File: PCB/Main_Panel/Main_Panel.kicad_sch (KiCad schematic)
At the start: 2 parts, among them U1 Pico, U2 TLC5947DAP

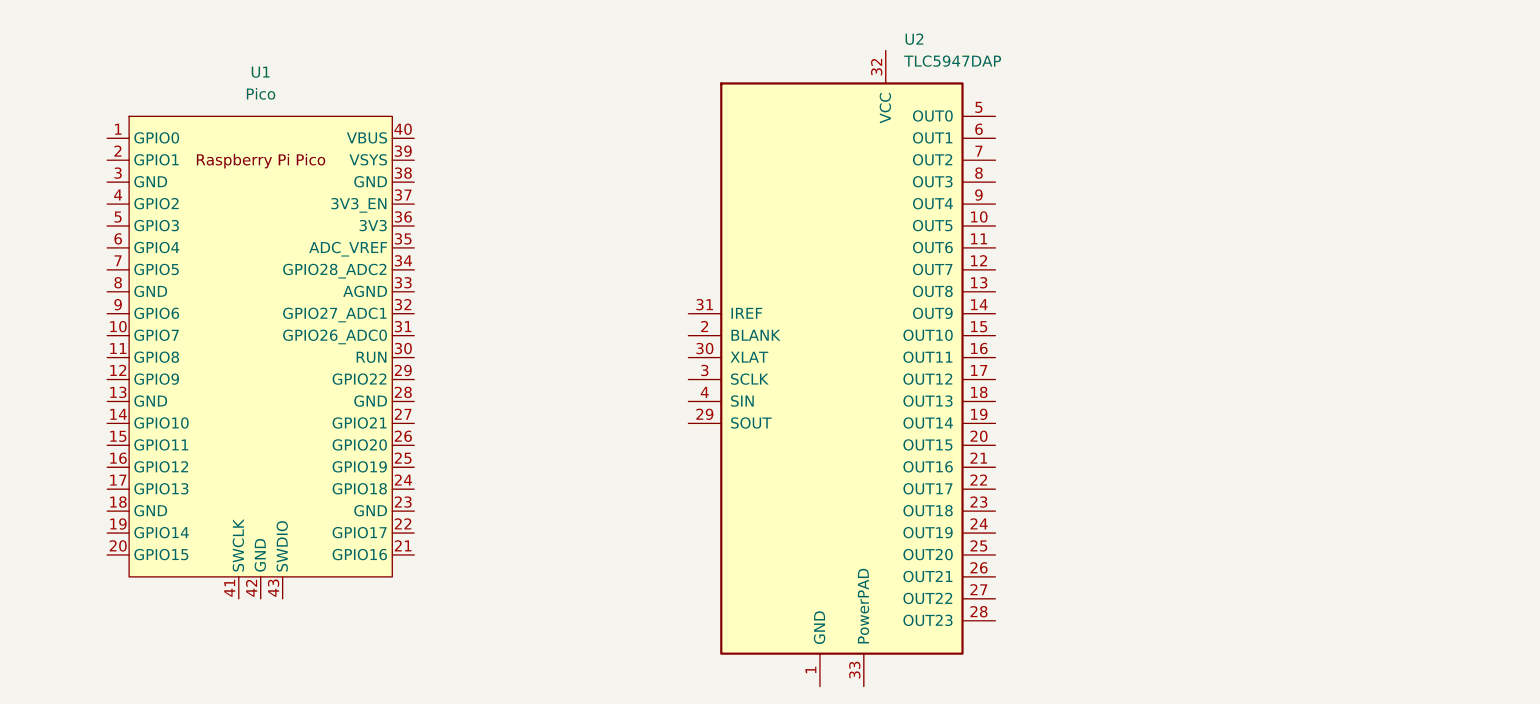
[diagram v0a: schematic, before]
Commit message: Fill kicad libraries
Finished the kicad symbol and footprint libraries and linked them together so everything works as intended.
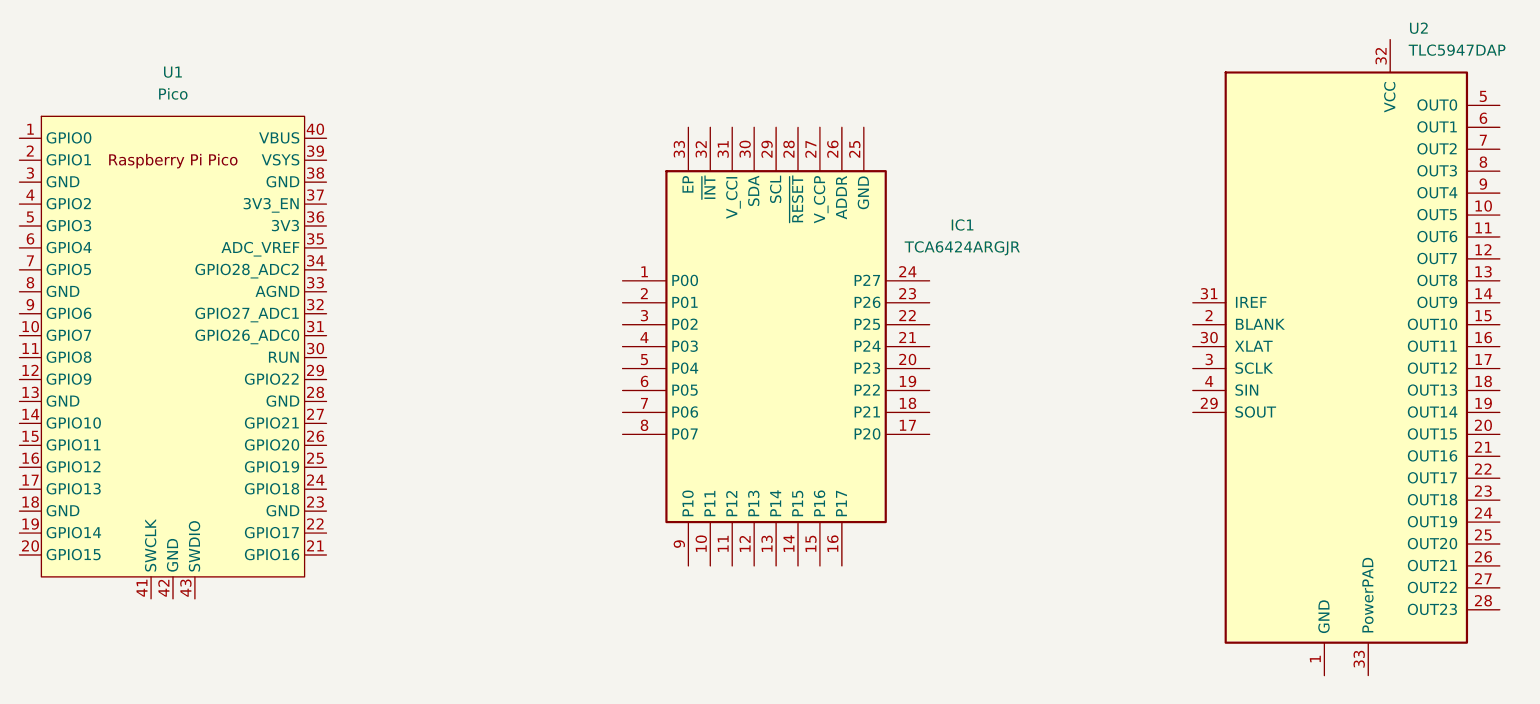
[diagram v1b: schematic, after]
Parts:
- added IC1: TCA6424ARGJR, Control_Panel_Footprints:QFN50P500X500X60-33N-D, symbol Control_Panel_Symbols:TCA6424ARGJR
- U1: footprint RPi_Pico:RPi_Pico_SMD_TH -> Control_Panel_Footprints:RPi_Pico_SMD_TH

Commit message: PCB Designs
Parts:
- added C1, C2, C3, C4: 0.01uF, Capacitor_SMD:C_0805_2012Metric, symbol Device:C_Small
- added H1, H10, H11, H12, H13, H14, H15, H16, H17, H18, H19, H2, H20, H21, H22, H3, H4, H5, H6, H7, H8, H9: MountingHole_Pad, MountingHole:MountingHole_3.2mm_M3_DIN965_Pad, symbol Mechanical:MountingHole_Pad
- added HS1: Heatsink_Pad, Control_Panel_Footprints:Heat Sink, symbol Mechanical:Heatsink_Pad
- added J1, J2: Conn_02x11_Odd_Even, Connector_PinHeader_2.54mm:PinHeader_2x11_P2.54mm_Vertical, symbol Connector_Generic:Conn_02x11_Odd_Even
- added J3, J4: Conn_01x05, Connector_PinHeader_2.54mm:PinHeader_1x05_P2.54mm_Vertical, symbol Connector_Generic:Conn_01x05
- added J5: Conn_01x15, Connector_PinHeader_2.54mm:PinHeader_1x15_P2.54mm_Vertical, symbol Connector_Generic:Conn_01x15
- added R1, R2, R3, R4: 10k, Resistor_SMD:R_0805_2012Metric, symbol Device:R
- added R30, R31, R32, R33, R34, R35, R36, R37: 10k, Resistor_SMD:R_0805_2012Metric, symbol Device:R_Small
- added R5: 2460, Resistor_SMD:R_0805_2012Metric, symbol Device:R_Small
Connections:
- net Encoder_0_B: now reaches U1.1 (GPIO0)
- net Encoder_0_B: now also C3.1, R36.2
- net Switch1: now reaches U1.10 (GPIO7)
- net Switch1: now also J5.3 (Pin_3)
- net GND: now reaches U1.13 (GND)
- net GND: now also IC1.25 (GND), IC1.26 (ADDR), U1.18 (GND), U1.23 (GND), U1.28 (GND), U1.3 (GND), U1.33 (AGND), U1.38 (GND), U1.8 (GND), U2.1 (GND), C1.2, C2.1, C3.2, C4.1, H1.1, H10.1, H11.1, H12.1, H13.1, H14.1, H15.1, H16.1, H17.1, H18.1, H19.1, H2.1, H20.1, H21.1, H22.1, H3.1, H4.1, H5.1, H6.1, H7.1, H8.1, H9.1, J1.21 (Pin_21), J1.22 (Pin_22), J2.21 (Pin_21), J2.22 (Pin_22), J3.3 (Pin_3), J4.1 (Pin_1), R5.1
- net Encoder_0_A: now reaches U1.2 (GPIO1)
- net Encoder_0_A: now also C4.2, R37.1
- net XLAT: now reaches U1.21 (GPIO16)
- net XLAT: now also U2.30 (XLAT)
- net Blank: now reaches U1.22 (GPIO17)
- net Blank: now also U2.2 (BLANK)
- net SCK: now reaches U1.24 (GPIO18)
- net SCK: now also U2.3 (SCLK)
- net MOSI: now reaches U1.25 (GPIO19)
- net MOSI: now also U2.4 (SIN)
- net Pot2: now reaches U1.31 (GPIO26_ADC0)
- net Pot2: now also J4.5 (Pin_5)
- net Pot1: now reaches U1.32 (GPIO27_ADC1)
- net Pot1: now also J4.4 (Pin_4)
- net Pot0: now reaches U1.34 (GPIO28_ADC2)
- net Pot0: now also J4.3 (Pin_3)
- net +3.3V: now reaches U1.36 (3V3)
- net +3.3V: now also IC1.27 (V_CCP), IC1.31 (V_CCI), U2.32 (VCC), J1.20 (Pin_20), J2.20 (Pin_20), J4.2 (Pin_2), J5.1 (Pin_1), R1.2, R2.2, R3.2, R30.1, R32.1, R34.1, R35.1, R4.2
- net +5V: now reaches U1.39 (VSYS)
- net +5V: now also U1.40 (VBUS), J1.19 (Pin_19), J2.19 (Pin_19)
- net Encoder_1_B: now reaches U1.4 (GPIO2)
- net Encoder_1_B: now also C1.1, R31.2
- net Encoder_1_A: now reaches U1.5 (GPIO3)
- net Encoder_1_A: now also C2.2, R33.1
- net SDA: now reaches U1.6 (GPIO4)
- net SDA: now also IC1.30 (SDA), R3.1
- net SCL: now reaches U1.7 (GPIO5)
- net SCL: now also IC1.29 (SCL), R2.1
- net Switch0: now reaches U1.9 (GPIO6)
- net Switch0: now also J5.2 (Pin_2)
- net Switch2: now reaches IC1.1 (P00)
- net Switch2: now also J5.4 (Pin_4)
- net Switch11: now reaches IC1.10 (P11)
- net Switch11: now also J5.13 (Pin_13)
- net Switch12: now reaches IC1.11 (P12)
- net Switch12: now also J5.14 (Pin_14)
- net Switch13: now reaches IC1.12 (P13)
- net Switch13: now also J5.15 (Pin_15)
- net Button0: now reaches IC1.13 (P14)
- net Button0: now also J1.1 (Pin_1)
- net Button1: now reaches IC1.14 (P15)
- net Button1: now also J1.3 (Pin_3)
- net Button2: now reaches IC1.15 (P16)
- net Button2: now also J1.5 (Pin_5)
- net Button3: now reaches IC1.16 (P17)
- net Button3: now also J1.7 (Pin_7)
- net Button4: now reaches IC1.17 (P20)
- net Button4: now also J1.9 (Pin_9)
- net Button5: now reaches IC1.18 (P21)
- net Button5: now also J1.11 (Pin_11)
- net Button6: now reaches IC1.19 (P22)
- net Button6: now also J2.1 (Pin_1)
- net Switch3: now reaches IC1.2 (P01)
- net Switch3: now also J5.5 (Pin_5)
- net Button7: now reaches IC1.20 (P23)
- net Button7: now also J2.3 (Pin_3)
- net Button8: now reaches IC1.21 (P24)
- net Button8: now also J2.5 (Pin_5)
- net Button9: now reaches IC1.22 (P25)
- net Button9: now also J2.7 (Pin_7)
- net Button10: now reaches IC1.23 (P26)
- net Button10: now also J2.9 (Pin_9)
- net Button11: now reaches IC1.24 (P27)
- net Button11: now also J2.11 (Pin_11)
- net at IC1.28 (~{RESET}): now also R1.1
- net Switch4: now reaches IC1.3 (P02)
- net Switch4: now also J5.6 (Pin_6)
- net at IC1.32 (~{INT}): now also R4.1
- net Switch5: now reaches IC1.4 (P03)
- net Switch5: now also J5.7 (Pin_7)
- net Switch6: now reaches IC1.5 (P04)
- net Switch6: now also J5.8 (Pin_8)
- net Switch7: now reaches IC1.6 (P05)
- net Switch7: now also J5.9 (Pin_9)
- net Switch8: now reaches IC1.7 (P06)
- net Switch8: now also J5.10 (Pin_10)
- net Switch9: now reaches IC1.8 (P07)
- net Switch9: now also J5.11 (Pin_11)
- net Switch10: now reaches IC1.9 (P10)
- net Switch10: now also J5.12 (Pin_12)
- net LED9: now reaches U2.10 (OUT5)
- net LED9: now also J1.14 (Pin_14)
- net LED8: now reaches U2.11 (OUT6)
- net LED8: now also J1.12 (Pin_12)
- net LED7: now reaches U2.12 (OUT7)
- net LED7: now also J1.10 (Pin_10)
- net LED6: now reaches U2.13 (OUT8)
- net LED6: now also J1.8 (Pin_8)
- net LED5: now reaches U2.14 (OUT9)
- net LED5: now also J1.6 (Pin_6)
- net LED4: now reaches U2.15 (OUT10)
- net LED4: now also J1.4 (Pin_4)
- net LED3: now reaches U2.16 (OUT11)
- net LED3: now also J1.2 (Pin_2)
- net LED12: now reaches U2.17 (OUT12)
- net LED12: now also J2.13 (Pin_13)
- net LED13: now reaches U2.18 (OUT13)
- net LED13: now also J2.15 (Pin_15)
- net LED14: now reaches U2.19 (OUT14)
- net LED14: now also J2.17 (Pin_17)
- net LED23: now reaches U2.20 (OUT15)
- net LED23: now also J2.18 (Pin_18)
- net LED22: now reaches U2.21 (OUT16)
- net LED22: now also J2.16 (Pin_16)
- net LED21: now reaches U2.22 (OUT17)
- net LED21: now also J2.14 (Pin_14)
- net LED20: now reaches U2.23 (OUT18)
- net LED20: now also J2.12 (Pin_12)
- net LED19: now reaches U2.24 (OUT19)
- net LED19: now also J2.10 (Pin_10)
- net LED18: now reaches U2.25 (OUT20)
- net LED18: now also J2.8 (Pin_8)
- net LED17: now reaches U2.26 (OUT21)
- net LED17: now also J2.6 (Pin_6)
- net LED16: now reaches U2.27 (OUT22)
- net LED16: now also J2.4 (Pin_4)
- net LED15: now reaches U2.28 (OUT23)
- net LED15: now also J2.2 (Pin_2)
- net at U2.31 (IREF): now also R5.2
- net at U2.33 (PowerPAD): now also HS1.1
- net LED0: now reaches U2.5 (OUT0)
- net LED0: now also J1.13 (Pin_13)
- net LED1: now reaches U2.6 (OUT1)
- net LED1: now also J1.15 (Pin_15)
- net LED2: now reaches U2.7 (OUT2)
- net LED2: now also J1.17 (Pin_17)
- net LED11: now reaches U2.8 (OUT3)
- net LED11: now also J1.18 (Pin_18)
- net LED10: now reaches U2.9 (OUT4)
- net LED10: now also J1.16 (Pin_16)
- new net: J3.4 (Pin_4), R31.1, R32.2
- new net: J3.1 (Pin_1), R34.2, R36.1
- new net: J3.2 (Pin_2), R35.2, R37.2
- new net: J3.5 (Pin_5), R30.2, R33.2
- no-connect marks 0 -> 19
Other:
- moved on the sheet: IC1, U1, U2

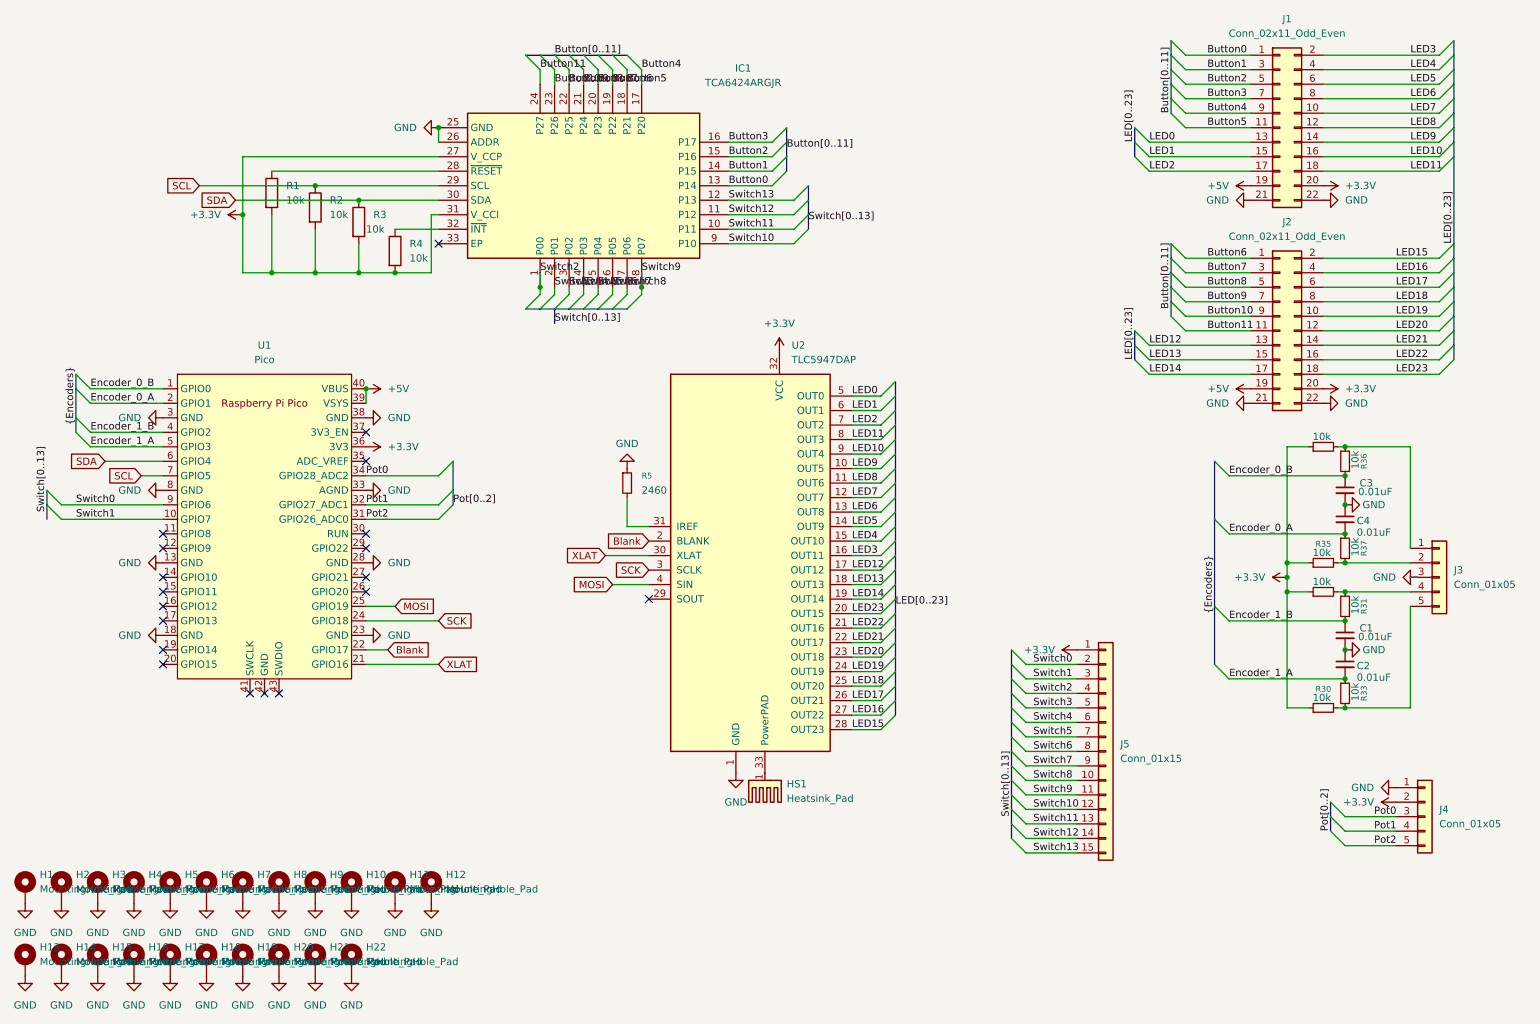
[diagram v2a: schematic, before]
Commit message: Update main and button pcbs to fix errors with v1.0
Added pull downs to gpio expander and changed header footprint
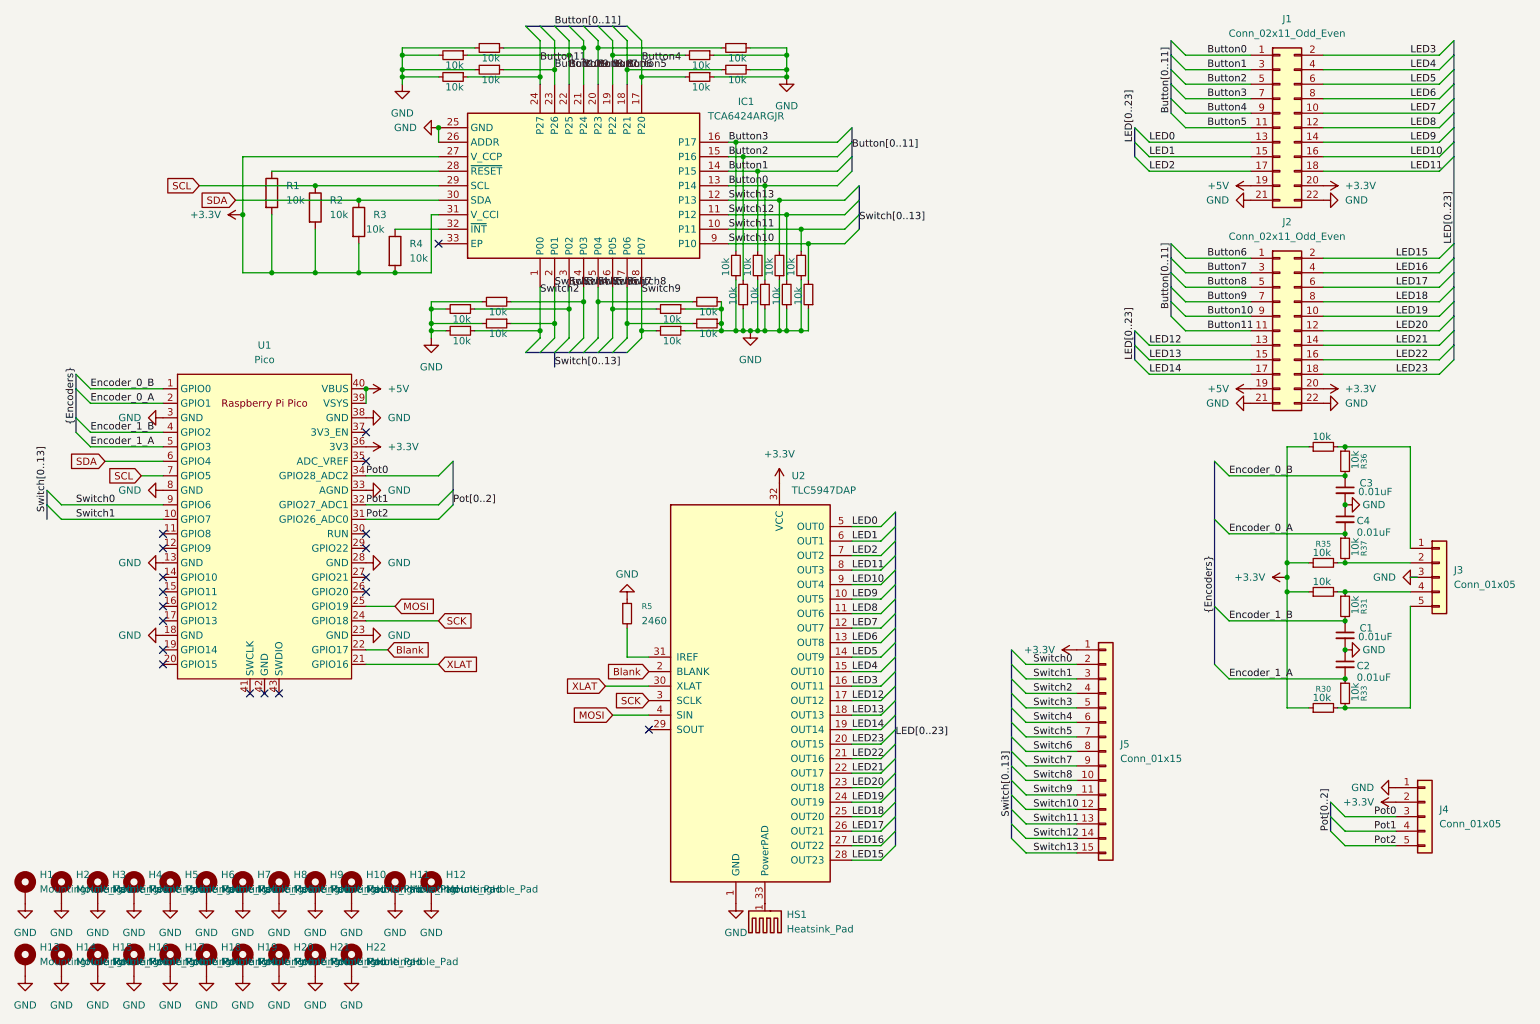
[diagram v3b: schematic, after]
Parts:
- added R10, R11, R12, R13, R14, R15, R16, R17, R18, R19, R20, R21, R22, R23, R24, R25, R26, R27, R28, R29, R6, R7, R8, R9: 10k, Resistor_SMD:R_0805_2012Metric, symbol Device:R_Small
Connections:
- net Button0: now also R10.2
- net Button1: now also R7.2
- net Button10: now also R16.1
- net Button11: now also R17.1
- net Button2: now also R9.2
- net Button3: now also R6.2
- net Button4: now also R19.2
- net Button5: now also R21.2
- net Button6: now also R18.2
- net Button7: now also R20.2
- net Button8: now also R15.1
- net Button9: now also R14.1
- net GND: now also R10.1, R11.1, R12.1, R13.1, R14.2, R15.2, R16.2, R17.2, R18.1, R19.1, R20.1, R21.1, R22.2, R23.2, R24.2, R25.2, R26.1, R27.1, R28.1, R29.1, R6.1, R7.1, R8.1, R9.1
- net Switch10: now also R13.2
- net Switch11: now also R12.2
- net Switch12: now also R11.2
- net Switch13: now also R8.2
- net Switch2: now also R23.1
- net Switch3: now also R25.1
- net Switch4: now also R22.1
- net Switch5: now also R24.1
- net Switch6: now also R28.2
- net Switch7: now also R26.2
- net Switch8: now also R29.2
- net Switch9: now also R27.2
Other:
- moved on the sheet: HS1, R5, U2
